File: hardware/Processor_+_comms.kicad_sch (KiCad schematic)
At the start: 50 parts, among them J1 53261-0471, U11 ATXMEGA256A3U-MH, U12 NTS0104, U13 CYPD3177, U14 TC1015-3.3VCT713

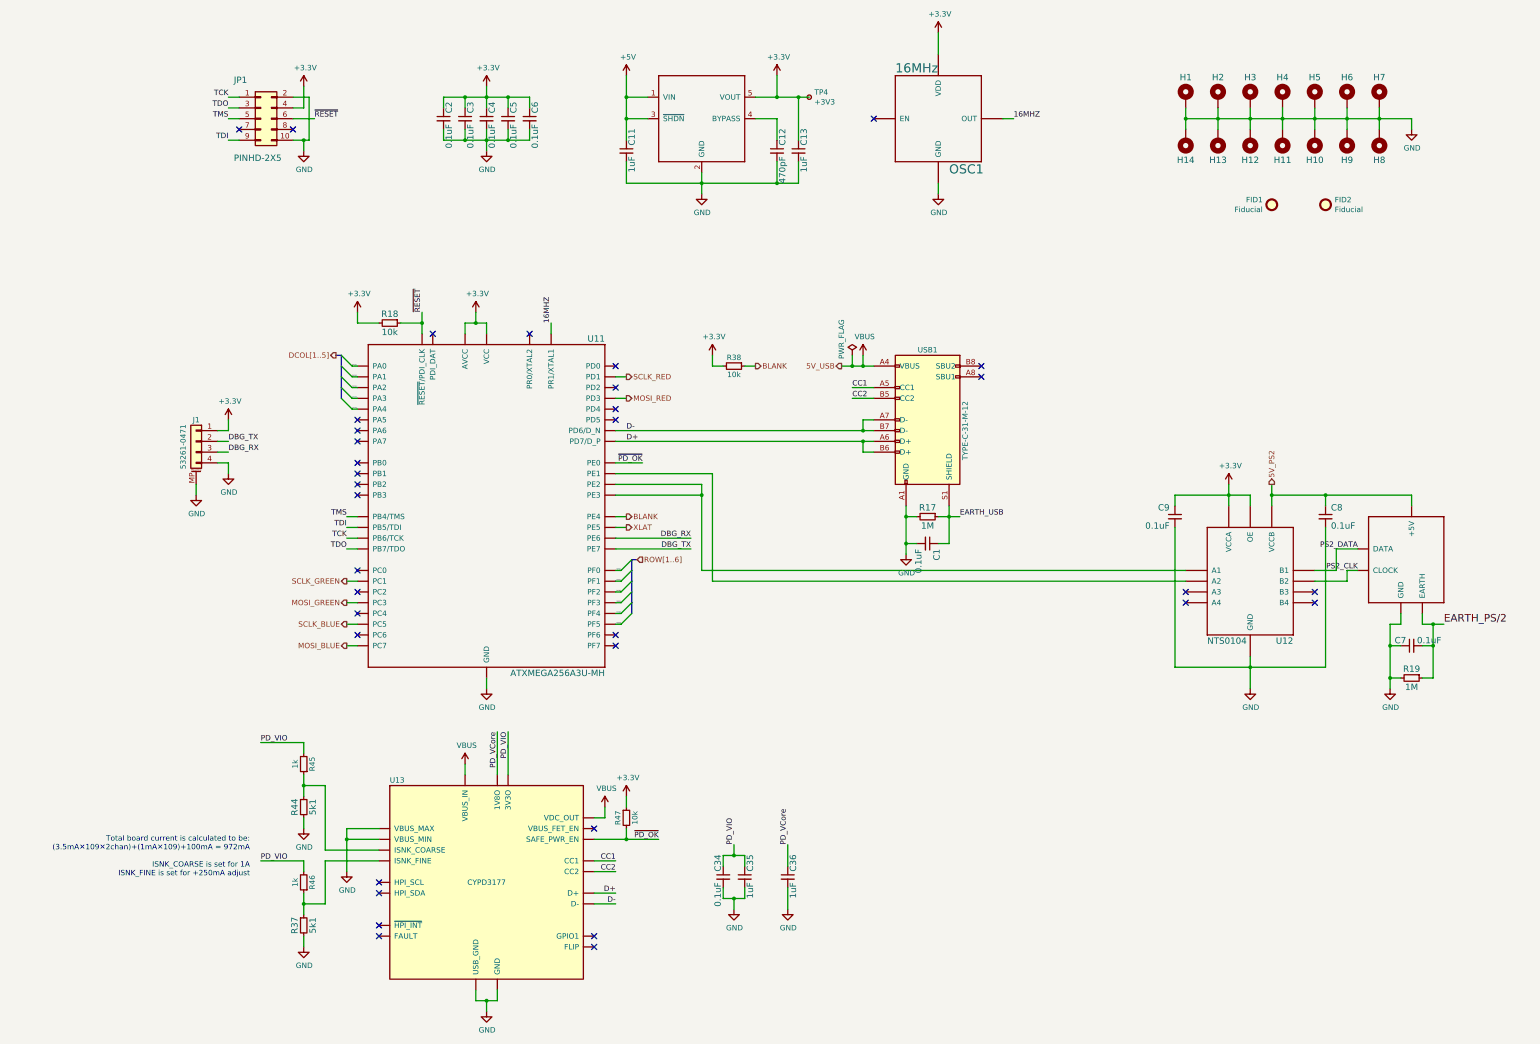
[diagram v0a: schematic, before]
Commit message: Improved a pile of the schematic, converting it to use KiCad schematic symbols and footprints instead of eagle imports
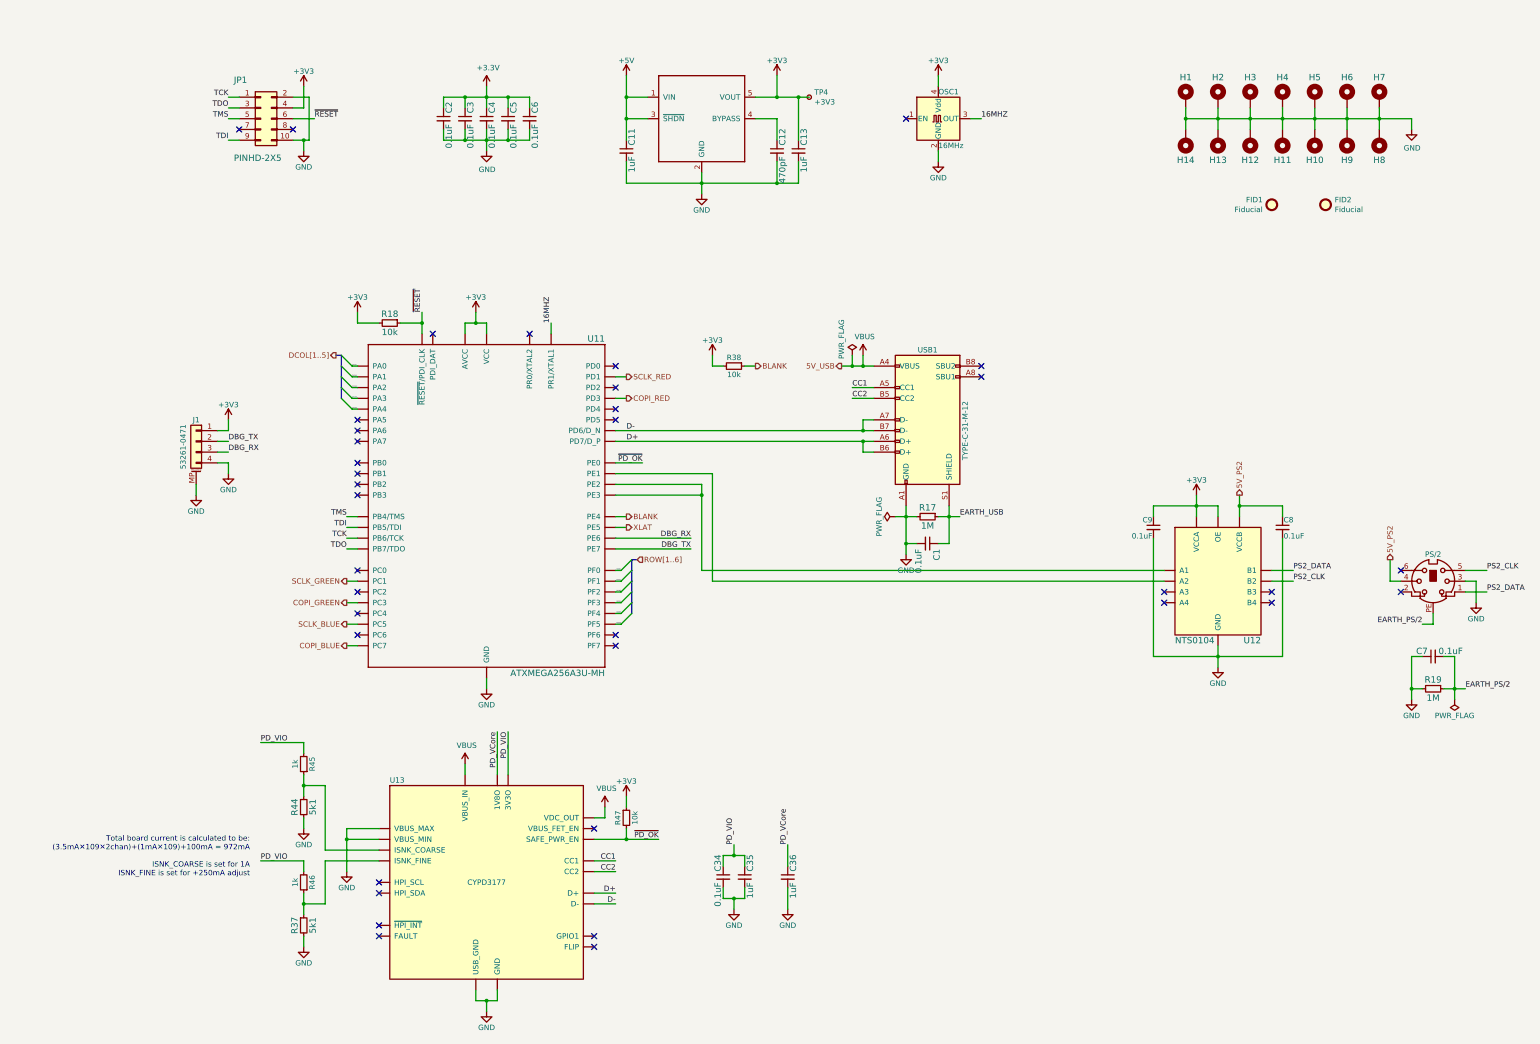
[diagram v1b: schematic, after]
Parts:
- removed PS/2: PS_2, MXKeyboard:TM_0508_A_6, symbol MXKeyboard-eagle-import:PS_2
- added PS/2: Mini-DIN-6, rhais_connector-lumberg:TM 0508 A_6, symbol DX-MON:Mini-DIN-6
- OSC1: symbol MXKeyboard-eagle-import:CXO-7M -> Oscillator:TXC-7C
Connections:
- net 5V_PS2: now also PS/2.4
- net GND: now also PS/2.3
- net PS2_CLK: now also PS/2.5
- net PS2_DATA: now also PS/2.1
- net EARTH_PS/2 renamed EARTH_PS/2
- net EARTH_PS/2: now also PS/2.PE
- net MOSI_BLUE renamed COPI_BLUE
- net MOSI_GREEN renamed COPI_GREEN
- net MOSI_RED renamed COPI_RED
- no-connect marks 35 -> 37
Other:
- moved on the sheet: C7, C8, C9, R19

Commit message: Further updates to the board files
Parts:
- U11: symbol MXKeyboard-eagle-import:ATXMEGA256A3U-MH -> DX-MON:ATXMEGA256A3U-MH
- U12: symbol MXKeyboard-eagle-import:NTS0104 -> DX-MON:NTS0104
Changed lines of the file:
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@@
     (pin "9")
   )
-  (symbol (lib_id "MXKeyboard-eagle-import:ATXMEGA256A3U-MH") (at 144.78 147.32 0) (unit 1)
-    (in_bom yes) (on_board yes)
-    (property "Reference" "U11" (id 0) (at 172.72 108.712 0)
-      (effects (font (size 1.4986 1.4986)) (justify right bottom))
-    )
-    (property "Value" "ATXMEGA256A3U-MH" (id 1) (at 172.72 185.928 0)
-      (effects (font (size 1.4986 1.4986)) (justify right top))
-    )
+  (symbol (lib_id "DX-MON:ATXMEGA256A3U-MH") (at 144.78 147.32 0) (unit 1)
+    (in_bom yes) (on_board yes)
+    (property "Reference" "U11" (id 0) (at 172.72 107.95 0)
+      (effects (font (size 1.27 1.27)) (justify right))
+    )
+    (property "Value" "ATXMEGA256A3U-MH" (id 1) (at 144.78 147.32 0))
     (property "Footprint" "rhais_package-qfn:QFN-64-1EP_9x9mm_P0.5mm_EP7.5x7.5mm" (id 2) (at 144.78 147.32 0)
       (effects (font (size 1.27 1.27)) hide)
@@
     (pin "5")
   )
-  (symbol (lib_id "MXKeyboard-eagle-import:NTS0104") (at 317.5 165.1 0) (unit 1)
+  (symbol (lib_id "DX-MON:NTS0104") (at 317.5 165.1 0) (unit 1)
     (in_bom yes) (on_board yes)
     (property "Reference" "U12" (id 0) (at 327.66 179.07 0)

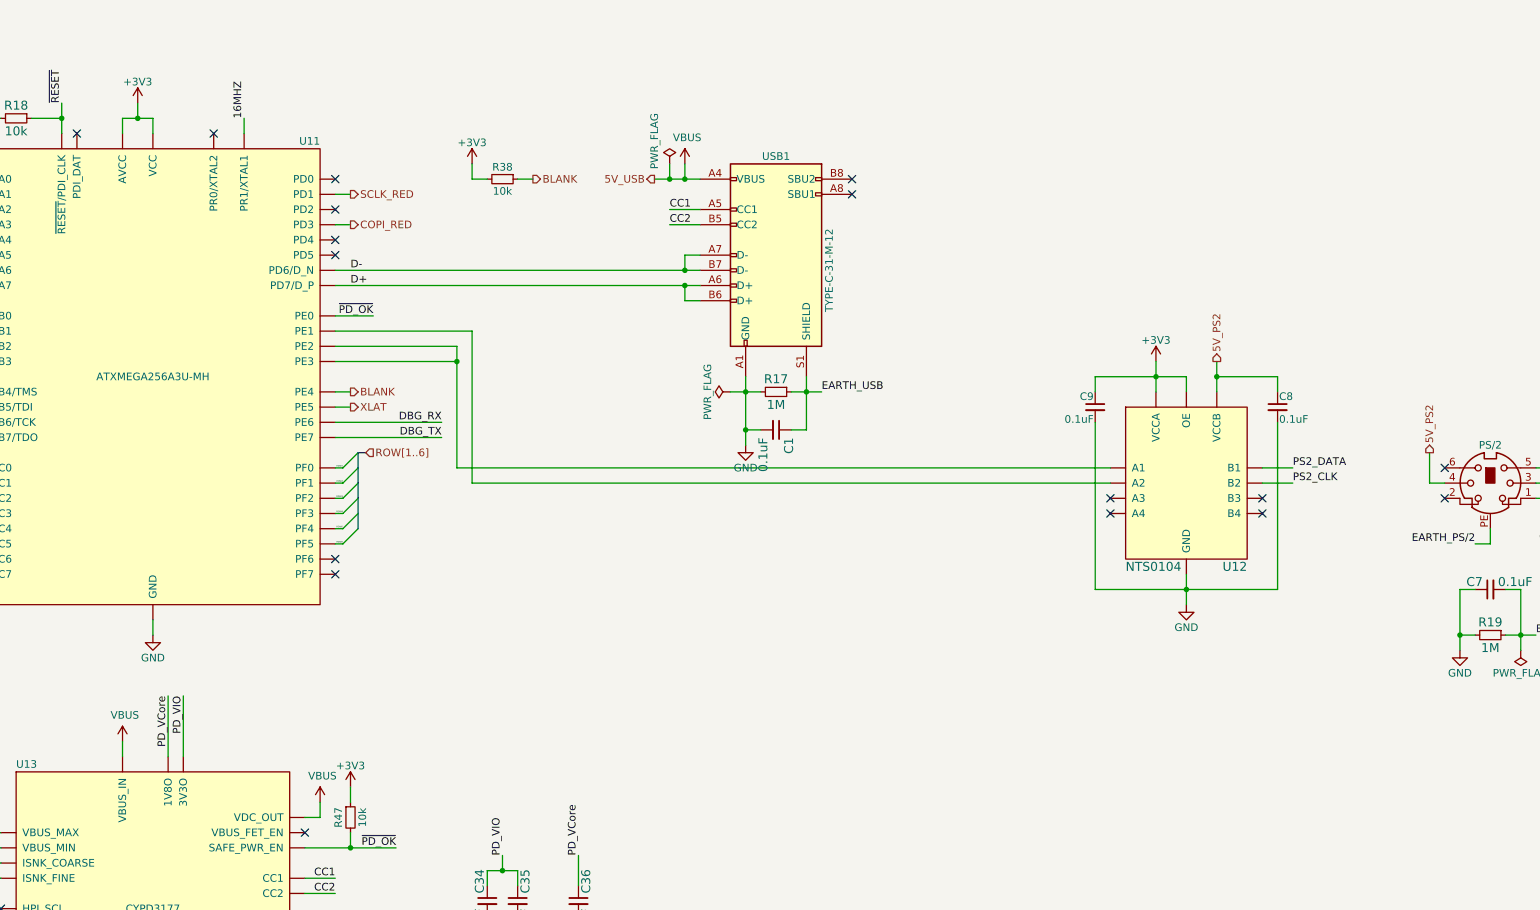
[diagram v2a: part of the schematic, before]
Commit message: More work on the schematics for the keyboard, including fixing all the page sizes after a mishap
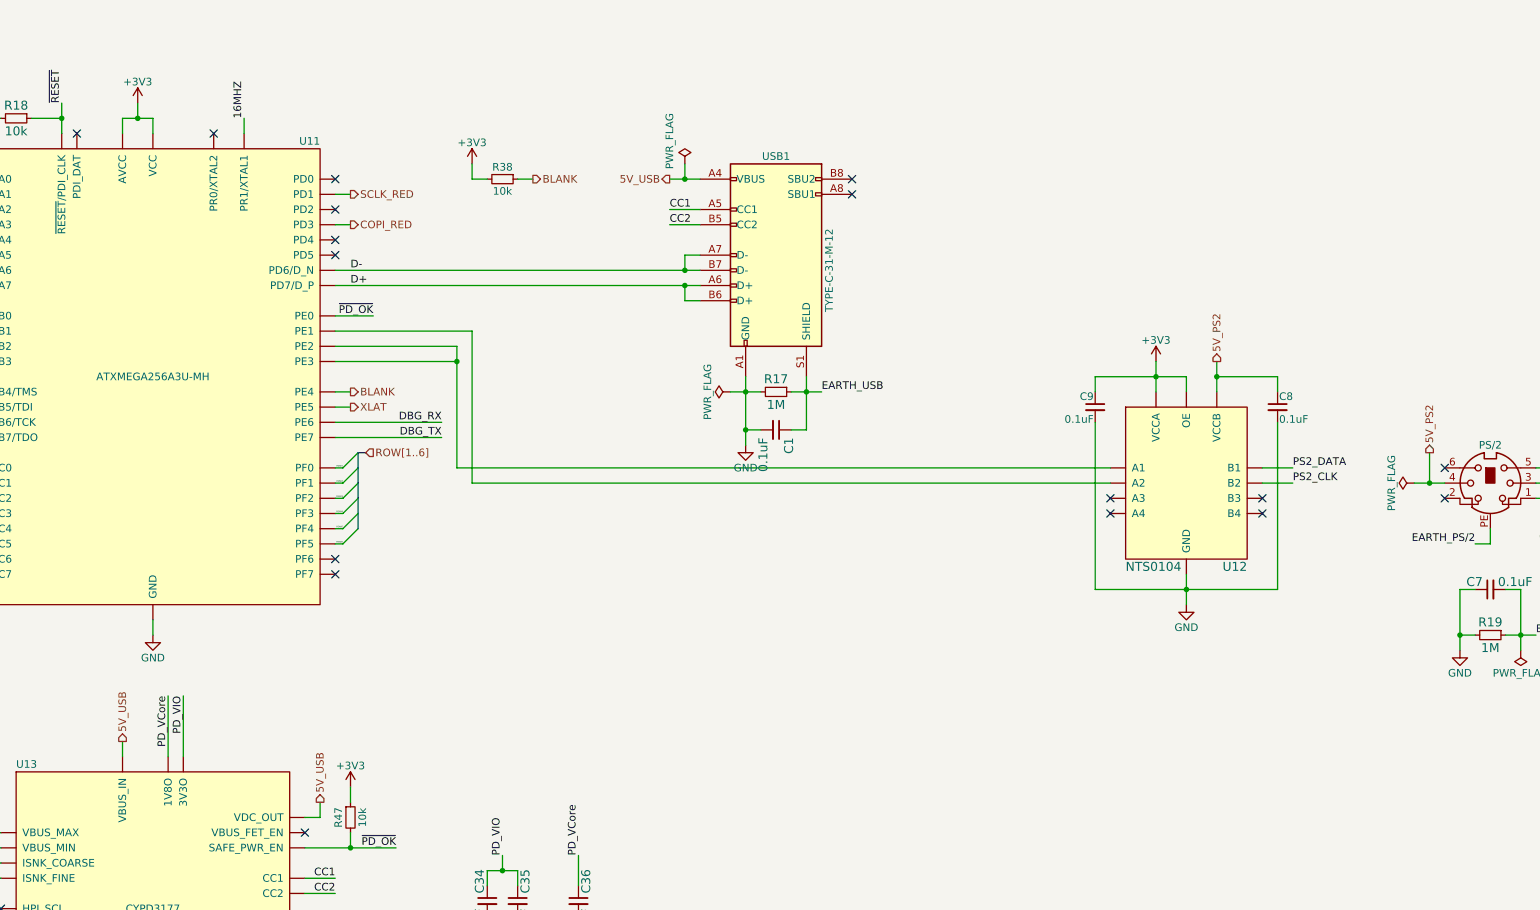
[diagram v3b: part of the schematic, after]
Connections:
- net VBUS renamed 5V_USB
